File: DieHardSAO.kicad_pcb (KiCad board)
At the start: 2 copper layers, 69.7 x 75.4 mm, 8 parts, among them X1 locked

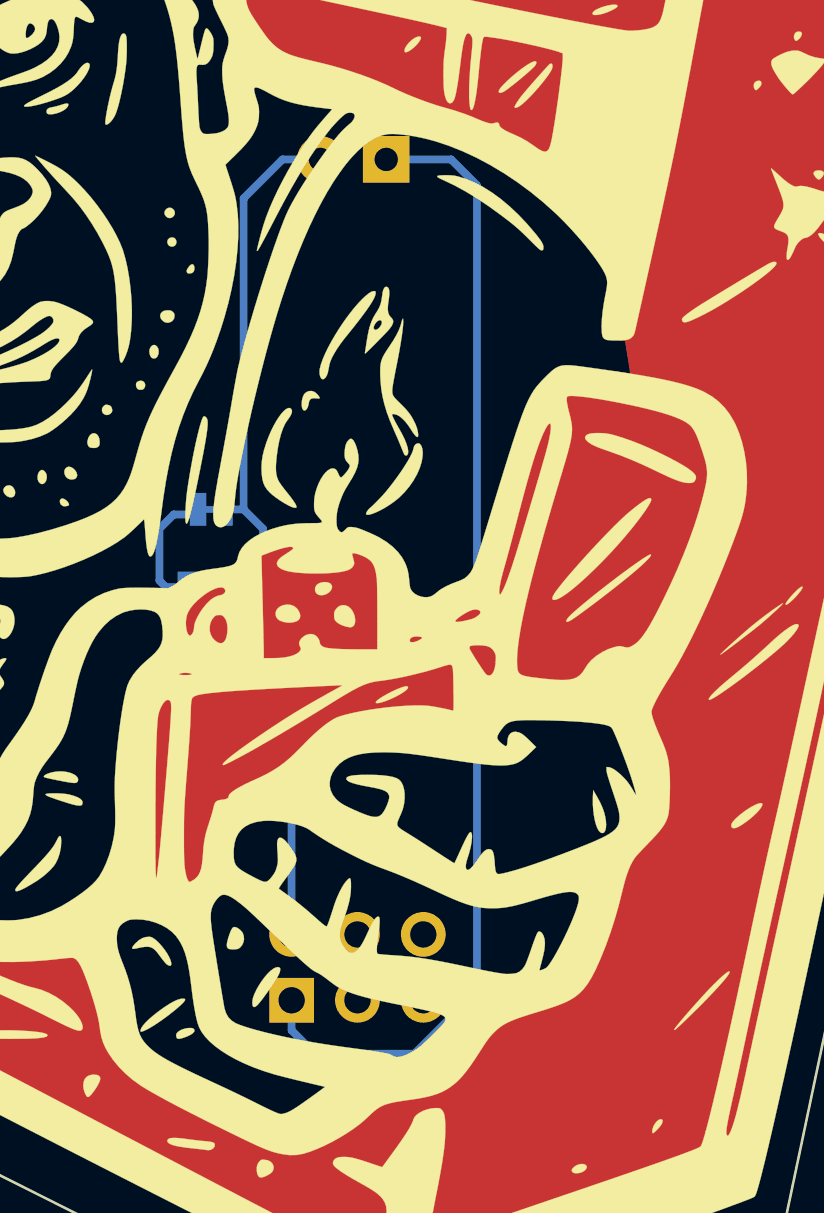
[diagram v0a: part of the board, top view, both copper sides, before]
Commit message: Changed jumper
Changed jumper and moved traces
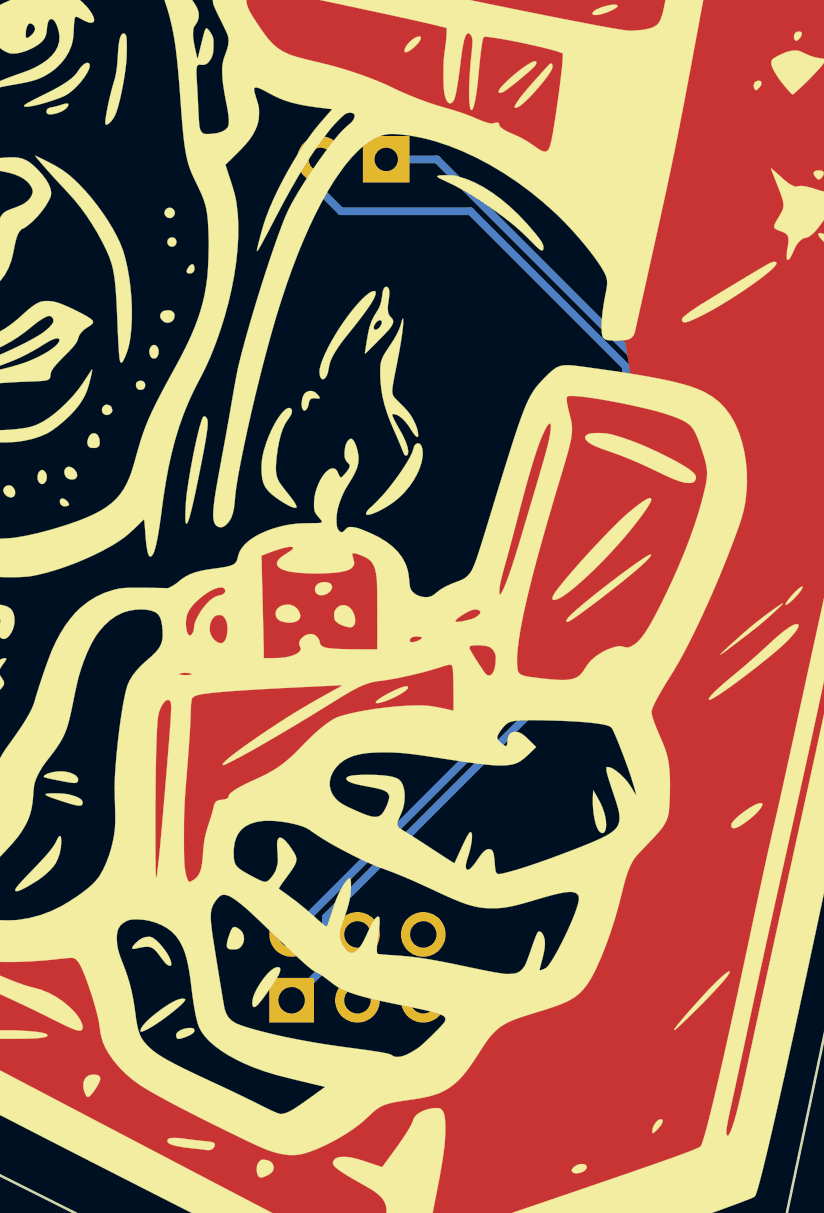
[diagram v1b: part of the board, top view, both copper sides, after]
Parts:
- JP1: value JUMPER-SMT_2_NC -> JUMPER-SMT_2_NO; footprint Jumpers:SMT-JUMPER_2_NC_TRACE_NO-SILK -> Jumper:SolderJumper-2_P1.3mm_Open_TrianglePad1.0x1.5mm
- moved R1 15.5 mm to (130.5, 102.8)
- moved JP1 15.3 mm to (130.3, 99.8)
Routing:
- net Net-(D1-Pad2): track 20.2 -> 24.2 mm
- net Net-(R1-Pad1): track 19.7 -> 21.5 mm
